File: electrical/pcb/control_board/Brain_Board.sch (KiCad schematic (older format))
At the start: 36 parts, among them J10 6posheader, J27 PEC10DAAN, J32 PPTC021LFBN-RC, J45 PPTC021LFBN-RC, J46 PPTC021LFBN-RC, J6 S9175-ND_rpi_breakout, J67 SSW-104-01-F-T, J7 S9175-ND_rpi_breakout, M1 Mounting_Holes, Q1 2N3906, Q2 2N3906, Q3 2N3906, SW1 CTS-206-124

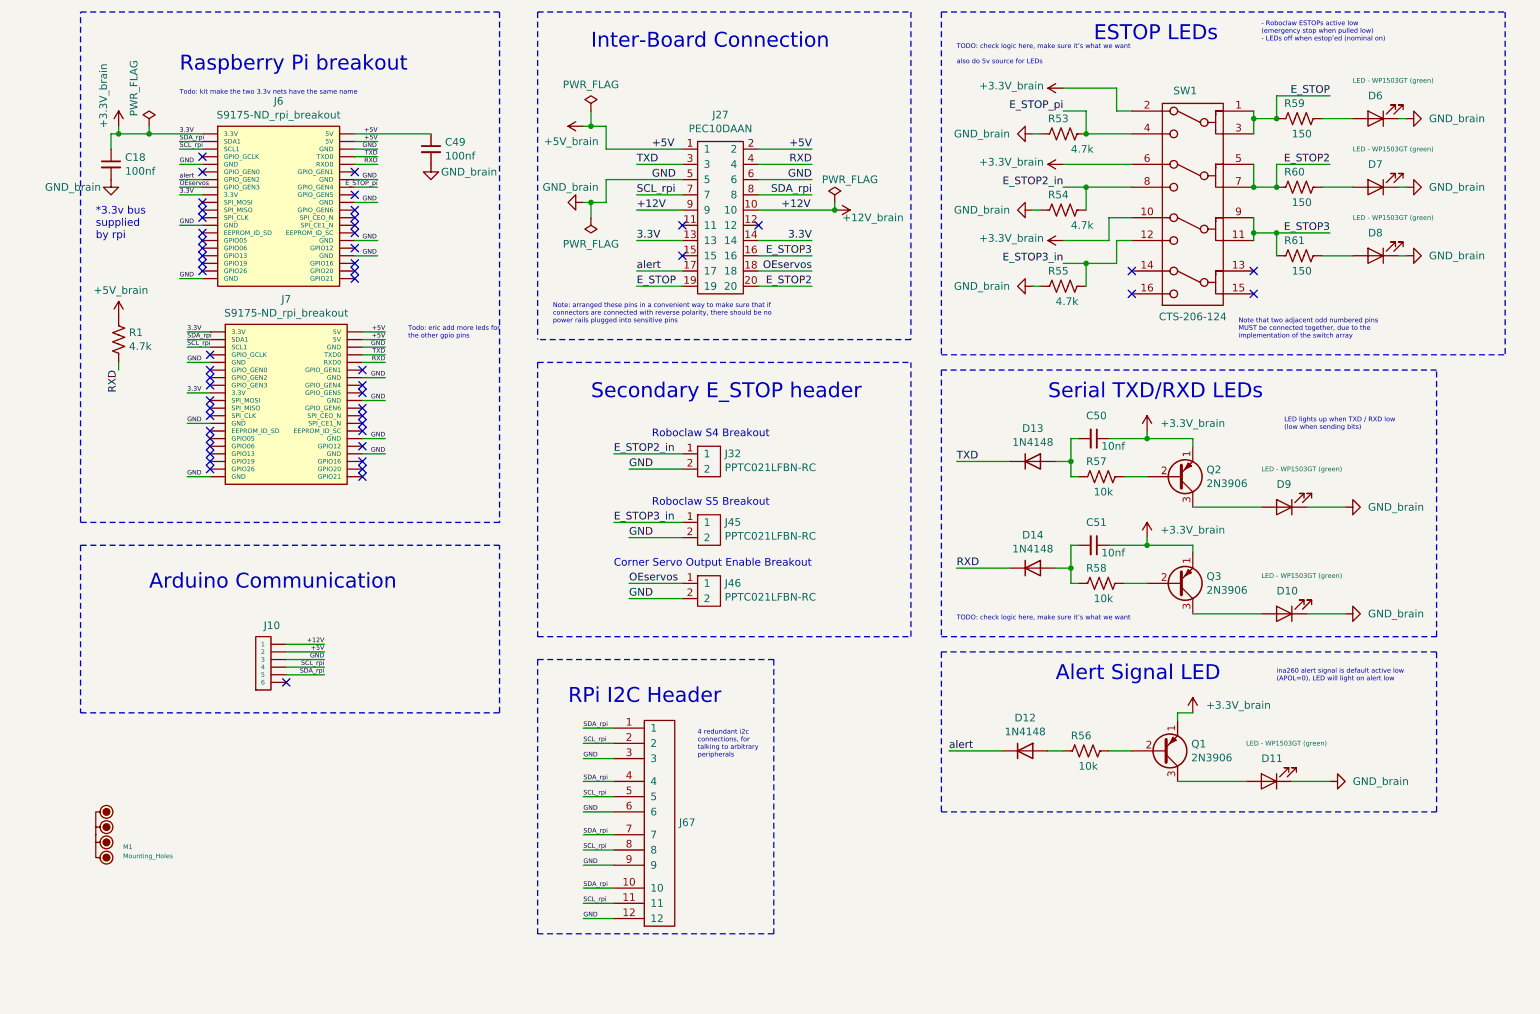
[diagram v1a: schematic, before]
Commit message: Clearing and redoing schematic designators
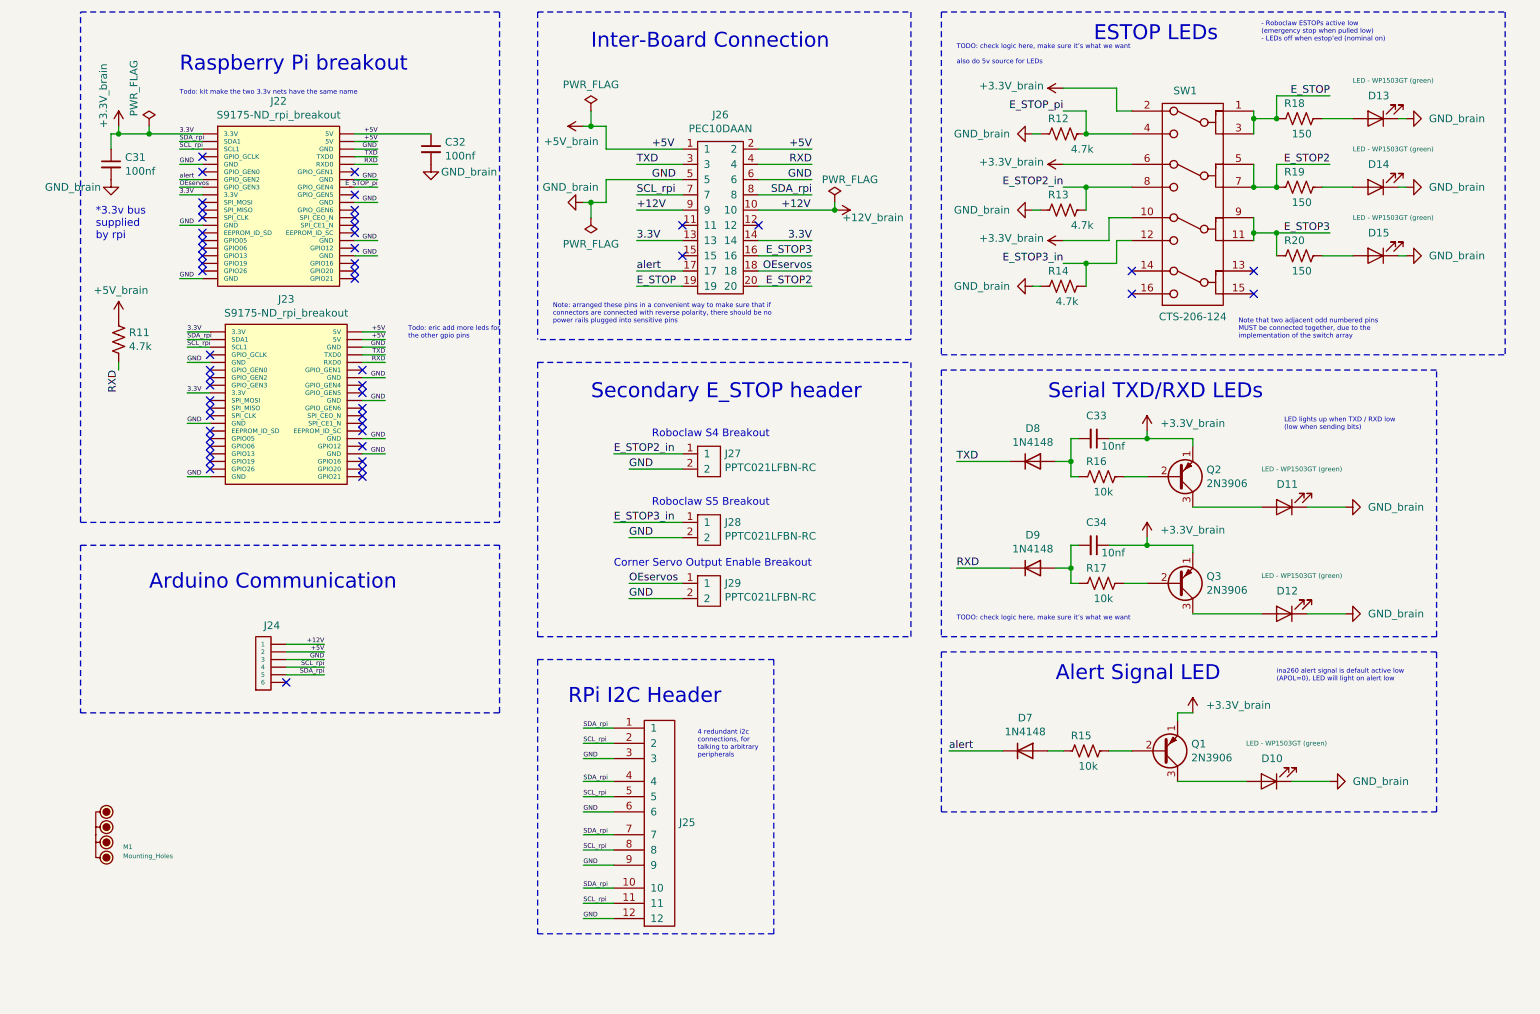
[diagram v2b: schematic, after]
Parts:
- renumbered C18 to C31, C49 to C32, C50 to C33, C51 to C34, D11 to D10, D9 to D11, D10 to D12, D6 to D13, D7 to D14, D8 to D15, D12 to D7, D13 to D8, D14 to D9, J6 to J22, J7 to J23, J10 to J24, J67 to J25, J27 to J26, J32 to J27, J45 to J28, J46 to J29, R1 to R11, R53 to R12, R54 to R13, R55 to R14, R56 to R15, R57 to R16, R58 to R17, R59 to R18, R60 to R19, R61 to R20

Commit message: More updates to initial pass of layout
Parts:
- removed D10, D11, D12, D13, D14, D15: LED - WP1503GT (green), LED_THT:LED_D5.0mm, symbol Device:LED
- added U6: DC7G3HWA, JPL Robotics:DC7G3HWA LED Array, symbol JPL_Robotics_Lib:DC7G3HWA
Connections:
- net GND_brain: now also U6.11, U6.12, U6.13, U6.14, U6.15, U6.16, U6.17, U6.18, U6.19, U6.20
- net ESTOP_LED_2: now reaches R19.1
- net ESTOP_LED_2: now also U6.9
- net ESTOP_LED_3: now reaches R20.1
- net ESTOP_LED_3: now also U6.8
- net TXD_LED: now reaches Q2.3 (C)
- net TXD_LED: now also U6.1
- net RXD_LED: now reaches Q3.3 (C)
- net RXD_LED: now also U6.2
- net ALERT_LED: now reaches Q1.3 (C)
- net ALERT_LED: now also U6.3
- net ESTOP_LED_1: now reaches R18.1
- net ESTOP_LED_1: now also U6.10
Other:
- moved on the sheet: J25

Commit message: Adding a large number of the 3d files for components
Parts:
- M1: footprint JPL Robotics:Raspberry pi footprint -> JPL Robotics:raspberry_pi_3b
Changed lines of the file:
@@
 F 0 "M1" V 1980 6329 30  0000 L CNN
 F 1 "Mounting_Holes" V 2040 6329 30  0000 L CNN
-F 2 "JPL Robotics:Raspberry pi footprint" H 1730 6330 30  0001 C CNN
+F 2 "JPL Robotics:raspberry_pi_3b" H 1730 6330 30  0001 C CNN
 F 3 "" H 1730 6330 30  0001 C CNN
 	1    1550 6150

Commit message: Adding the rest of the 3D components to PCB
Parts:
- J26: footprint JPL Robotics:PEC10DAAN -> JPL Robotics:WM6548-ND
- SW1: value CTS-206-124 -> CT206124-ND
- U6: footprint JPL Robotics:DC7G3HWA LED Array -> JPL Robotics:DC7G3HWA_led_array
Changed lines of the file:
@@
 F 0 "J26" H 5650 1925 50  0000 C CNN
 F 1 "PEC10DAAN" H 5650 1834 50  0000 C CNN
-F 2 "JPL Robotics:PEC10DAAN" H 5950 1850 50  0001 C CNN
+F 2 "JPL Robotics:WM6548-ND" H 5950 1850 50  0001 C CNN
 F 3 "" H 5950 1850 50  0001 C CNN
 	1    5650 1850
@@
 P 8550 3150
 F 0 "SW1" H 8700 4683 50  0000 C CNN
-F 1 "CTS-206-124" H 8750 3200 50  0000 C CNN
+F 1 "CT206124-ND" H 8750 3200 50  0000 C CNN
 F 2 "JPL Robotics:CTS-206-124" H 8550 3150 50  0001 C CNN
 F 3 "" H 8550 3150 50  0001 C CNN
@@
 F 0 "U6" H 5700 7665 50  0000 C CNN
 F 1 "DC7G3HWA" H 5700 7574 50  0000 C CNN
-F 2 "JPL Robotics:DC7G3HWA LED Array" H 5150 6650 50  0001 C CNN
+F 2 "JPL Robotics:DC7G3HWA_led_array" H 5150 6650 50  0001 C CNN
 F 3 "" H 5150 6650 50  0001 C CNN
 	1    5150 6650

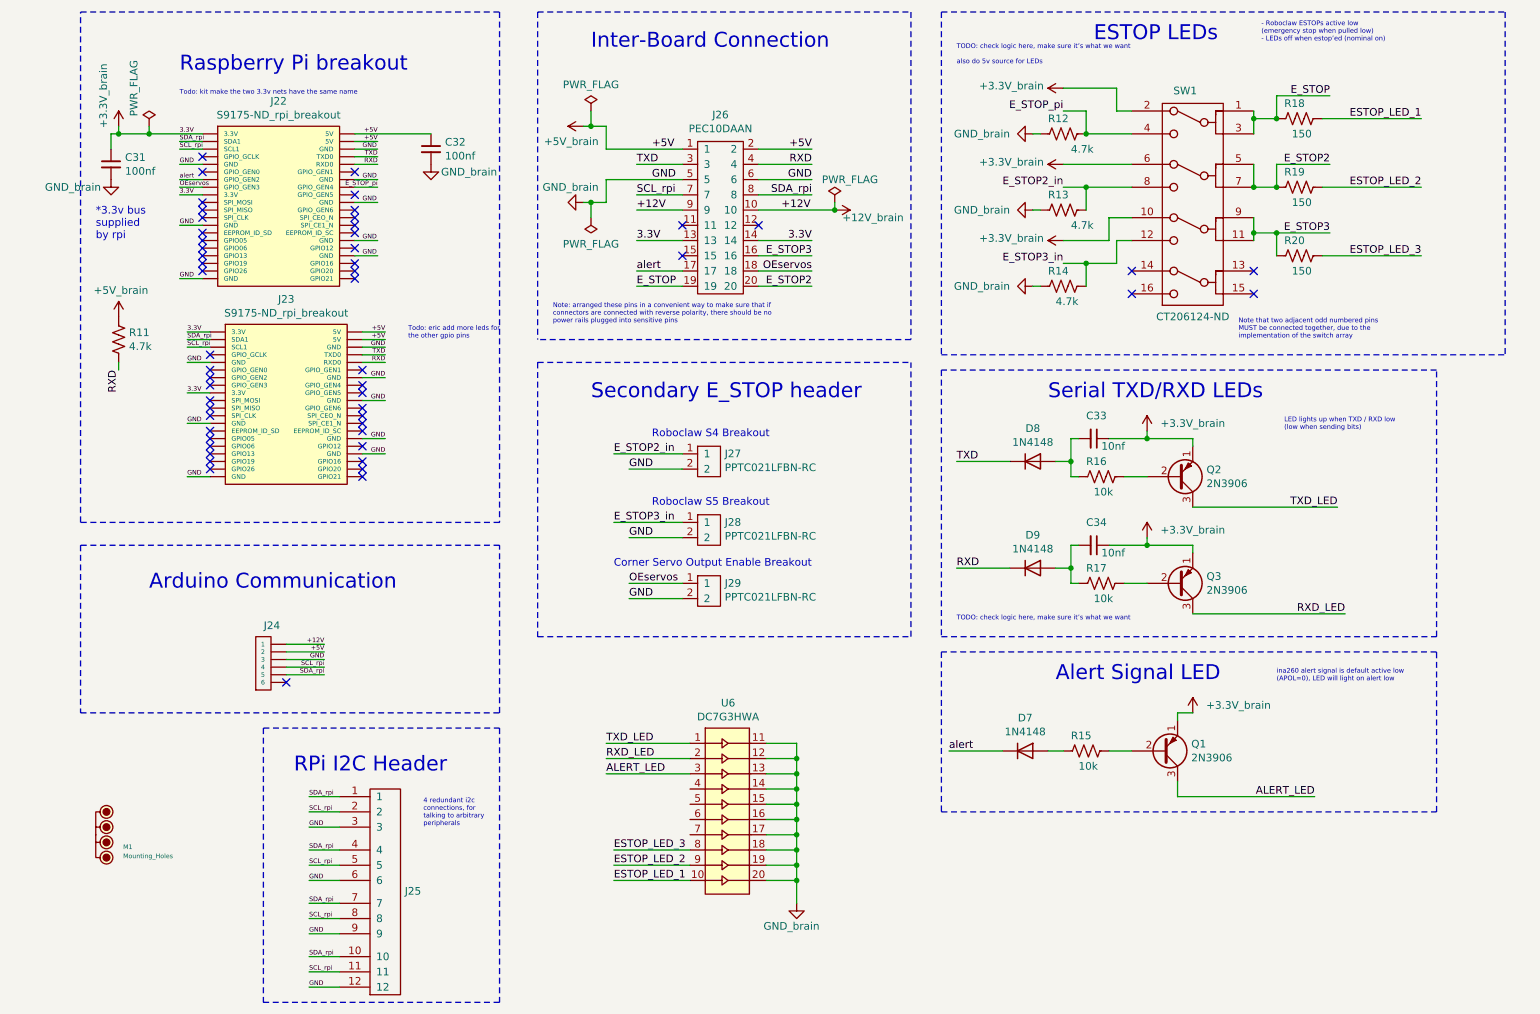
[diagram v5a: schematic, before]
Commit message: Cleaning up a bunch of electrical rules check violations in the schematic
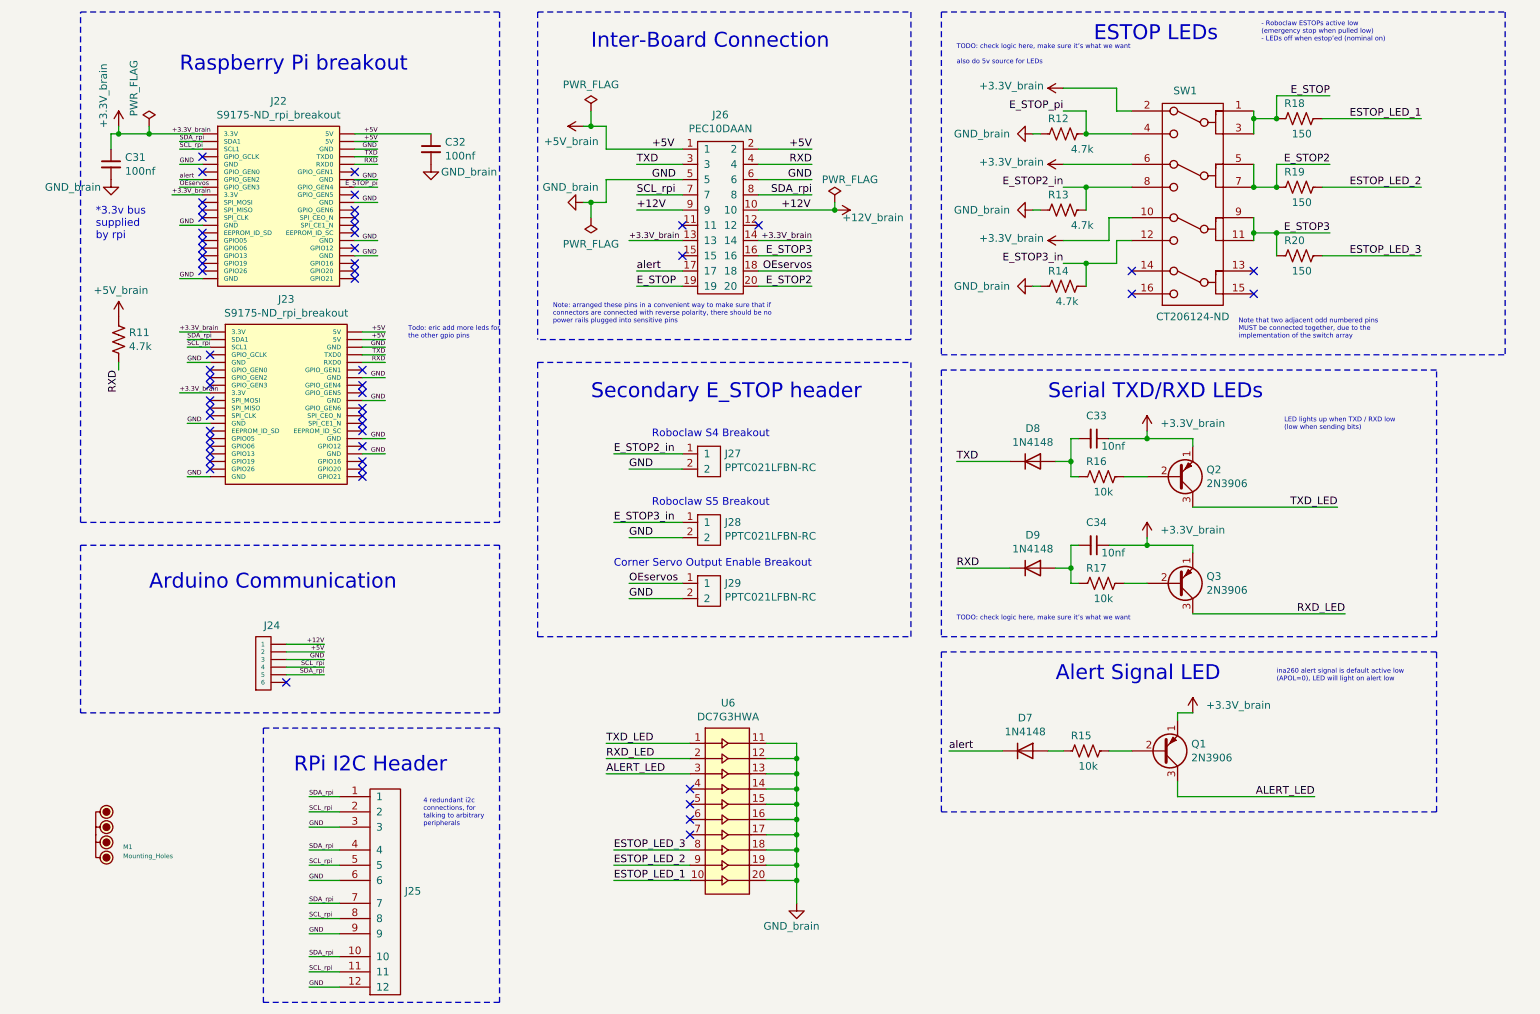
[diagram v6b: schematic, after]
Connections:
- no-connect marks 53 -> 57
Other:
- note removed: "Todo: kit make the two 3.3v nets have the same name"
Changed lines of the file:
@@
 EESchema Schematic File Version 4
-LIBS:Control_Boards-cache
-EELAYER 26 0
+EELAYER 30 0
 EELAYER END
 $Descr A4 11693 8268
@@
 	2250 2100 2100 2100
 Wire Wire Line
-	2250 2300 2100 2300
-Wire Wire Line
 	2250 2500 2100 2500
 Wire Wire Line
@@
 Wire Wire Line
 	3400 2700 3250 2700
-Text Label 2100 1900 0    30   ~ 0
-3.3V
-Text Label 2100 2300 0    30   ~ 0
-3.3V
+Text Label 2050 2300 0    30   ~ 0
++3.3V_brain
 Text Label 3400 1900 2    30   ~ 0
 +5V
@@
 $EndComp
 Wire Wire Line
-	2300 3200 2150 3200
-Wire Wire Line
 	2300 3400 2150 3400
 Wire Wire Line
-	2300 3600 2150 3600
-Wire Wire Line
 	2300 3800 2150 3800
 Wire Wire Line
@@
 Wire Wire Line
 	3450 4000 3300 4000
-Text Label 2150 3200 0    30   ~ 0
-3.3V
+Text Label 2100 3200 0    30   ~ 0
++3.3V_brain
 Text Label 2150 3400 0    30   ~ 0
 GND
-Text Label 2150 3600 0    30   ~ 0
-3.3V
+Text Label 2100 3600 0    30   ~ 0
++3.3V_brain
 Text Label 2150 3800 0    30   ~ 0
 GND
@@
 NoConn ~ 5900 2500
 NoConn ~ 5400 2700
-Wire Wire Line
-	5400 2600 5100 2600
-Text Label 5100 2600 0    50   ~ 0
-3.3V
-Text Label 6250 2600 2    50   ~ 0
-3.3V
+Text Label 5050 2600 0    39   ~ 0
++3.3V_brain
+Text Label 6250 2600 2    39   ~ 0
++3.3V_brain
 Wire Wire Line
 	5900 2600 6250 2600
@@
 Text Notes 9200 1300 0    31   ~ 0
 - Roboclaw ESTOPs active low \n(emergency stop when pulled low)\n- LEDs off when estop’ed (nominal on)
-Text Notes 2100 1650 0    31   ~ 0
-Todo: kit make the two 3.3v nets have the same name
 Text Notes 7200 1450 0    31   ~ 0
 TODO: check logic here, make sure it’s what we want\n\nalso do 5v source for LEDs
@@
 U 1 1 61D7BA49
 P 3350 7650
+AR Path="/61D7BA49" Ref="J25"  Part="1"
+AR Path="/60A5279E/61D7BA49" Ref="J25"  Part="1"
 F 0 "J25" H 3578 8430 50  0000 L CNN
 F 1 "SSW-104-01-F-T" H 3578 8385 50  0001 L CNN
@@
 Wire Wire Line
 	6150 6000 6150 6100
+Text Label 2050 1900 0    30   ~ 0
++3.3V_brain
+Wire Wire Line
+	5050 2600 5400 2600
+Wire Wire Line
+	2050 2300 2250 2300
+Wire Wire Line
+	2100 3200 2300 3200
+Wire Wire Line
+	2100 3600 2300 3600
+NoConn ~ 5450 6200
+NoConn ~ 5450 6300
+NoConn ~ 5450 6400
+NoConn ~ 5450 6500
 $EndSCHEMATC

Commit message: Finished rev2 layout for motor board
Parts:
- added MH10, MH11, MH12, MH9: #6THRU-HOLE, JPL Robotics:#6THRU-HOLE, symbol JPL_Robotics_Lib:#6THRU-HOLE
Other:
- note added: "For mounting to motor board"
- note added: "RPi mounting holes"
- note added: "\n"
- moved on the sheet: M1
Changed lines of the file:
@@
 L JPL_Robotics_Lib:Mounting_Holes M?
 U 1 1 61DB5332
-P 1550 6150
+P 1400 5900
 AR Path="/60A51BAC/61DB5332" Ref="M?"  Part="1"
 AR Path="/60A5279E/61DB5332" Ref="M1"  Part="1"
-F 0 "M1" V 1980 6329 30  0000 L CNN
-F 1 "Mounting_Holes" V 2040 6329 30  0000 L CNN
-F 2 "JPL Robotics:raspberry_pi_3b" H 1730 6330 30  0001 C CNN
-F 3 "" H 1730 6330 30  0001 C CNN
-	1    1550 6150
+F 0 "M1" V 1830 6079 30  0000 L CNN
+F 1 "Mounting_Holes" V 1890 6079 30  0000 L CNN
+F 2 "JPL Robotics:raspberry_pi_3b" H 1580 6080 30  0001 C CNN
+F 3 "" H 1580 6080 30  0001 C CNN
+	1    1400 5900
 	0    1    1    0
 $EndComp
@@
 NoConn ~ 5450 6400
 NoConn ~ 5450 6500
+Text Notes 1850 7400 0    50   ~ 0
+\n
+$Comp
+L JPL_Robotics_Lib:#6THRU-HOLE MH?
+U 1 1 626D877C
+P 1450 6800
+AR Path="/60A51BAC/626D877C" Ref="MH?"  Part="1"
+AR Path="/60A5279E/626D877C" Ref="MH9"  Part="1"
+F 0 "MH9" H 1581 6800 30  0000 L CNN
+F 1 "#6THRU-HOLE" H 1450 6940 30  0001 C CNN
+F 2 "JPL Robotics:#6THRU-HOLE" H 1450 6890 30  0001 C CNN
+F 3 "" H 1450 6890 30  0001 C CNN
+	1    1450 6800
+	1    0    0    -1
+$EndComp
+$Comp
+L JPL_Robotics_Lib:#6THRU-HOLE MH?
+U 1 1 626D8782
+P 1450 6950
+AR Path="/60A51BAC/626D8782" Ref="MH?"  Part="1"
+AR Path="/60A5279E/626D8782" Ref="MH10"  Part="1"
+F 0 "MH10" H 1581 6950 30  0000 L CNN
+F 1 "#6THRU-HOLE" H 1450 7090 30  0001 C CNN
+F 2 "JPL Robotics:#6THRU-HOLE" H 1450 7040 30  0001 C CNN
+F 3 "" H 1450 7040 30  0001 C CNN
+	1    1450 6950
+	1    0    0    -1
+$EndComp
+$Comp
+L JPL_Robotics_Lib:#6THRU-HOLE MH?
+U 1 1 626D8788
+P 1450 7100
+AR Path="/60A51BAC/626D8788" Ref="MH?"  Part="1"
+AR Path="/60A5279E/626D8788" Ref="MH11"  Part="1"
+F 0 "MH11" H 1581 7100 30  0000 L CNN
+F 1 "#6THRU-HOLE" H 1450 7240 30  0001 C CNN
+F 2 "JPL Robotics:#6THRU-HOLE" H 1450 7190 30  0001 C CNN
+F 3 "" H 1450 7190 30  0001 C CNN
+	1    1450 7100
+	1    0    0    -1
+$EndComp
+$Comp
+L JPL_Robotics_Lib:#6THRU-HOLE MH?
+U 1 1 626D878E
+P 1450 7250
+AR Path="/60A51BAC/626D878E" Ref="MH?"  Part="1"
+AR Path="/60A5279E/626D878E" Ref="MH12"  Part="1"
+F 0 "MH12" H 1581 7250 30  0000 L CNN
+F 1 "#6THRU-HOLE" H 1450 7390 30  0001 C CNN
+F 2 "JPL Robotics:#6THRU-HOLE" H 1450 7340 30  0001 C CNN
+F 3 "" H 1450 7340 30  0001 C CNN
+	1    1450 7250
+	1    0    0    -1
+$EndComp
+Text Notes 1200 6700 0    31   ~ 0
+For mounting to motor board
+Text Notes 1150 6000 0    31   ~ 0
+RPi mounting holes
 $EndSCHEMATC
